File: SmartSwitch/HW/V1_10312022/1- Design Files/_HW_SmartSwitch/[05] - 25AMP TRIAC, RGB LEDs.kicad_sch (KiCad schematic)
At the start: 6 parts

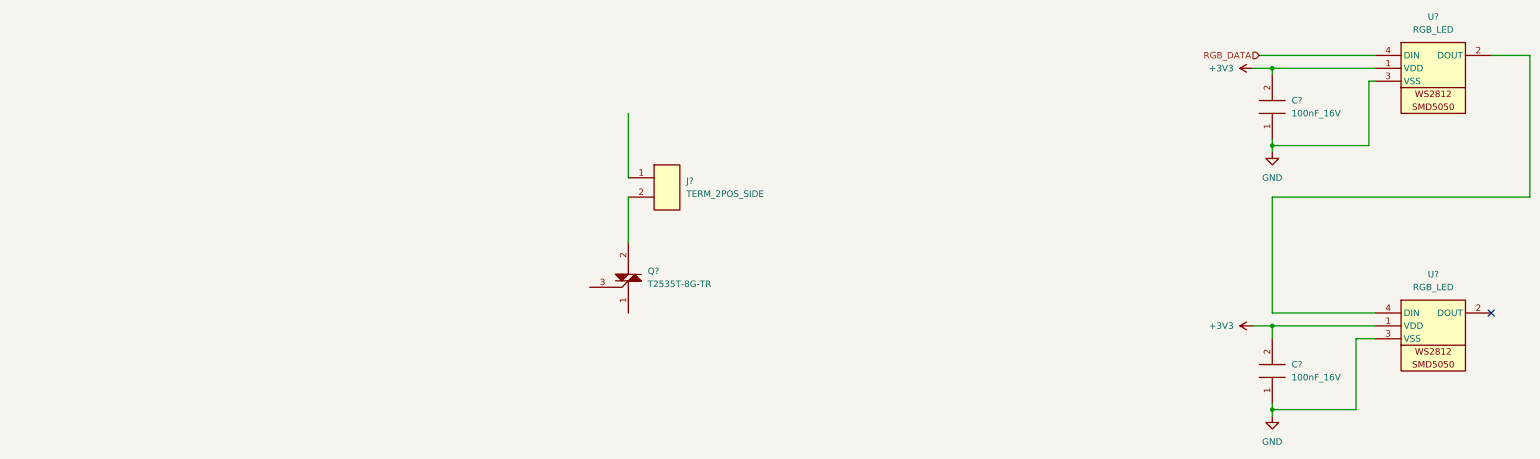
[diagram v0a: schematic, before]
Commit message: Current sensor has been done almost :D
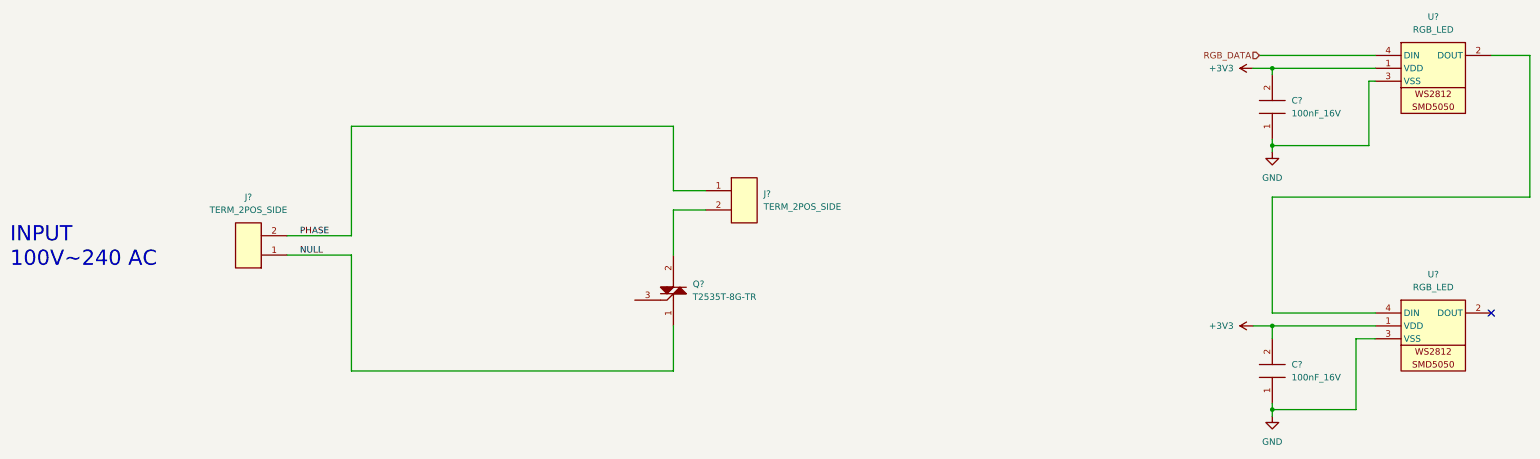
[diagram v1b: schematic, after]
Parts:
- added J?: TERM_2POS_SIDE, TerminalBlock_Phoenix:TerminalBlock_Phoenix_MKDS-1,5-2_1x02_P5.00mm_Horizontal, symbol SmartSwitch:TERM_2POS_SIDE
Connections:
- net PHASE: now reaches J?.1
- net PHASE: now also J?.2
- net NULL: now reaches Q?.1
- net NULL: now also J?.1
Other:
- note added: "INPUT 100V~240 AC"
- moved on the sheet: J?, Q?
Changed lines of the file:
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@@
   )
   (no_connect (at 335.28 149.86))
+  (wire (pts (xy 97.79 134.62) (xy 110.49 134.62))
+    (stroke (width 0) (type default) (color 0 0 0 0))
+  )
   (wire (pts (xy 289.56 99.06) (xy 312.42 99.06))
     (stroke (width 0) (type default) (color 0 0 0 0))
   )
+  (wire (pts (xy 180.34 125.73) (xy 173.99 125.73))
+    (stroke (width 0) (type default) (color 0 0 0 0))
+  )
   (wire (pts (xy 311.15 116.84) (xy 292.1 116.84))
     (stroke (width 0) (type default) (color 0 0 0 0))
   )
+  (wire (pts (xy 110.49 134.62) (xy 110.49 113.03))
+    (stroke (width 0) (type default) (color 0 0 0 0))
+  )
   (wire (pts (xy 292.1 149.86) (xy 312.42 149.86))
     (stroke (width 0) (type default) (color 0 0 0 0))
@@
     (stroke (width 0) (type default) (color 0 0 0 0))
   )
-  (wire (pts (xy 165.1 110.49) (xy 165.1 123.19))
+  (wire (pts (xy 173.99 125.73) (xy 173.99 113.03))
+    (stroke (width 0) (type default) (color 0 0 0 0))
+  )
+  (wire (pts (xy 110.49 161.29) (xy 173.99 161.29))
     (stroke (width 0) (type default) (color 0 0 0 0))
   )
@@
     (stroke (width 0) (type default) (color 0 0 0 0))
   )
-  (wire (pts (xy 165.1 127) (xy 165.1 135.89))
-    (stroke (width 0) (type default) (color 0 0 0 0))
-  )
   (wire (pts (xy 342.9 127) (xy 292.1 127))
     (stroke (width 0) (type default) (color 0 0 0 0))
   )
+  (wire (pts (xy 97.79 138.43) (xy 110.49 138.43))
+    (stroke (width 0) (type default) (color 0 0 0 0))
+  )
+  (wire (pts (xy 173.99 161.29) (xy 173.99 152.4))
+    (stroke (width 0) (type default) (color 0 0 0 0))
+  )
+  (wire (pts (xy 180.34 129.54) (xy 173.99 129.54))
+    (stroke (width 0) (type default) (color 0 0 0 0))
+  )
   (wire (pts (xy 312.42 104.14) (xy 311.15 104.14))
     (stroke (width 0) (type default) (color 0 0 0 0))
@@
     (stroke (width 0) (type default) (color 0 0 0 0))
   )
+  (wire (pts (xy 173.99 129.54) (xy 173.99 138.43))
+    (stroke (width 0) (type default) (color 0 0 0 0))
+  )
   (wire (pts (xy 288.29 152.4) (xy 292.1 152.4))
     (stroke (width 0) (type default) (color 0 0 0 0))
   )
+  (wire (pts (xy 110.49 113.03) (xy 173.99 113.03))
+    (stroke (width 0) (type default) (color 0 0 0 0))
+  )
   (wire (pts (xy 335.28 99.06) (xy 342.9 99.06))
     (stroke (width 0) (type default) (color 0 0 0 0))
@@
   (wire (pts (xy 292.1 101.6) (xy 292.1 102.87))
     (stroke (width 0) (type default) (color 0 0 0 0))
+  )
+  (wire (pts (xy 110.49 138.43) (xy 110.49 161.29))
+    (stroke (width 0) (type default) (color 0 0 0 0))
+  )
+  (text "INPUT\n100V~240 AC\n" (at 43.18 140.97 0)
+    (effects (font (size 3 3)) (justify left bottom))
+  )
+  (label "PHASE" (at 100.33 134.62 0)
+    (effects (font (size 1.27 1.27)) (justify left bottom))
+  )
+  (label "NULL" (at 100.33 138.43 0)
+    (effects (font (size 1.27 1.27)) (justify left bottom))
   )
   (hierarchical_label "RGB_DATA" (shape input) (at 289.56 99.06 180)
@@
     (pin "4")
   )
+  (symbol (lib_id "SmartSwitch:TERM_2POS_SIDE") (at 92.71 140.97 180) (unit 1)
+    (in_bom yes) (on_board yes) (fields_autoplaced)
+    (property "Reference" "J?" (id 0) (at 90.17 127 0))
+    (property "Value" "TERM_2POS_SIDE" (id 1) (at 90.17 129.54 0))
+    (property "Footprint" "TerminalBlock_Phoenix:TerminalBlock_Phoenix_MKDS-1,5-2_1x02_P5.00mm_Horizontal" (id 2) (at 50.8 151.13 0)
+      (effects (font (size 1.27 1.27)) hide)
+    )
+    (property "Datasheet" "https://www.we-online.com/katalog/datasheet/691137710002.pdf" (id 3) (at 60.96 146.05 0)
+      (effects (font (size 1.27 1.27)) hide)
+    )
+    (property "Description" "TERM BLK 2POS SIDE ENTRY 5MM PCB" (id 4) (at 74.93 148.59 0)
+      (effects (font (size 1.27 1.27)) hide)
+    )
+    (pin "1")
+    (pin "2")
+  )
   (symbol (lib_id "power:GND") (at 292.1 118.11 0) (unit 1)
     (in_bom yes) (on_board yes) (fields_autoplaced)
@@
     (pin "1")
   )
-  (symbol (lib_id "SmartSwitch:TERM_2POS_SIDE") (at 170.18 120.65 0) (unit 1)
-    (in_bom yes) (on_board yes) (fields_autoplaced)
-    (property "Reference" "J?" (id 0) (at 176.53 123.8249 0)
-      (effects (font (size 1.27 1.27)) (justify left))
-    )
-    (property "Value" "TERM_2POS_SIDE" (id 1) (at 176.53 126.3649 0)
-      (effects (font (size 1.27 1.27)) (justify left))
-    )
-    (property "Footprint" "TerminalBlock_Phoenix:TerminalBlock_Phoenix_MKDS-1,5-2_1x02_P5.00mm_Horizontal" (id 2) (at 212.09 110.49 0)
-      (effects (font (size 1.27 1.27)) hide)
-    )
-    (property "Datasheet" "https://www.we-online.com/katalog/datasheet/691137710002.pdf" (id 3) (at 201.93 115.57 0)
-      (effects (font (size 1.27 1.27)) hide)
-    )
-    (property "Description" "TERM BLK 2POS SIDE ENTRY 5MM PCB" (id 4) (at 187.96 113.03 0)
-      (effects (font (size 1.27 1.27)) hide)
-    )
-    (pin "1")
-    (pin "2")
-  )
-  (symbol (lib_id "SmartSwitch:T2535T-8G-TR") (at 157.48 135.89 0) (unit 1)
-    (in_bom yes) (on_board yes) (fields_autoplaced)
-    (property "Reference" "Q?" (id 0) (at 168.91 141.6049 0)
-      (effects (font (size 1.27 1.27)) (justify left))
-    )
-    (property "Value" "T2535T-8G-TR" (id 1) (at 168.91 144.1449 0)
-      (effects (font (size 1.27 1.27)) (justify left))
-    )
-    (property "Footprint" "Package_TO_SOT_SMD:TO-263-2" (id 2) (at 173.99 123.19 0)
-      (effects (font (size 1.27 1.27)) hide)
-    )
-    (property "Datasheet" "https://www.st.com/resource/en/datasheet/t2535t-8g.pdf" (id 3) (at 186.69 125.73 0)
-      (effects (font (size 1.27 1.27)) hide)
-    )
-    (property "Description" "TRIAC Standard 800 V 25 A Surface Mount D²PAK" (id 4) (at 181.61 128.27 0)
-      (effects (font (size 1.27 1.27)) hide)
-    )
+  (symbol (lib_id "SmartSwitch:TERM_2POS_SIDE") (at 185.42 123.19 0) (unit 1)
+    (in_bom yes) (on_board yes) (fields_autoplaced)
+    (property "Reference" "J?" (id 0) (at 191.77 126.3649 0)
+      (effects (font (size 1.27 1.27)) (justify left))
+    )
+    (property "Value" "TERM_2POS_SIDE" (id 1) (at 191.77 128.9049 0)
+      (effects (font (size 1.27 1.27)) (justify left))
+    )
+    (property "Footprint" "TerminalBlock_Phoenix:TerminalBlock_Phoenix_MKDS-1,5-2_1x02_P5.00mm_Horizontal" (id 2) (at 227.33 113.03 0)
+      (effects (font (size 1.27 1.27)) hide)
+    )
+    (property "Datasheet" "https://www.we-online.com/katalog/datasheet/691137710002.pdf" (id 3) (at 217.17 118.11 0)
+      (effects (font (size 1.27 1.27)) hide)
+    )
+    (property "Description" "TERM BLK 2POS SIDE ENTRY 5MM PCB" (id 4) (at 203.2 115.57 0)
+      (effects (font (size 1.27 1.27)) hide)
+    )
+    (pin "1")
+    (pin "2")
+  )
+  (symbol (lib_id "SmartSwitch:T2535T-8G-TR") (at 166.37 138.43 0) (unit 1)
+    (in_bom yes) (on_board yes) (fields_autoplaced)
+    (property "Reference" "Q?" (id 0) (at 177.8 144.1449 0)
+      (effects (font (size 1.27 1.27)) (justify left))
+    )
+    (property "Value" "T2535T-8G-TR" (id 1) (at 177.8 146.6849 0)
+      (effects (font (size 1.27 1.27)) (justify left))
+    )
+    (property "Footprint" "Package_TO_SOT_SMD:TO-263-2" (id 2) (at 182.88 125.73 0)
+      (effects (font (size 1.27 1.27)) hide)
+    )
+    (property "Datasheet" "https://www.st.com/resource/en/datasheet/t2535t-8g.pdf" (id 3) (at 195.58 128.27 0)
+      (effects (font (size 1.27 1.27)) hide)
+    )
+    (property "Description" "TRIAC Standard 800 V 25 A Surface Mount D²PAK" (id 4) (at 190.5 130.81 0)
+      (effects (font (size 1.27 1.27)) hide)
+    )

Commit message: Current and Voltage sampler
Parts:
- removed C? (x2): 100nF_16V, Capacitor_SMD:C_0402_1005Metric, symbol SmartSwitch:100nF_16V
- removed J? (x2): TERM_2POS_SIDE, TerminalBlock_Phoenix:TerminalBlock_Phoenix_MKDS-1,5-2_1x02_P5.00mm_Horizontal, symbol SmartSwitch:TERM_2POS_SIDE
- removed Q?: T2535T-8G-TR, Package_TO_SOT_SMD:TO-263-2, symbol SmartSwitch:T2535T-8G-TR
- removed U? (x2): RGB_LED, LED_SMD:LED_WS2812B_PLCC4_5.0x5.0mm_P3.2mm, symbol SmartSwitch:RGB_LED
- added J?: IEC-EW-4, symbol SmartSwitch:IEC-EW-4
- added J?: PX0675/PC, symbol SmartSwitch:PX0675/PC
- added Q?: T2535T-8G-TR, Package_TO_SOT_SMD:TO-263-2, symbol SmartSwitch:T2535T-8G-TR
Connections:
- net NULL: now also J?.3 (N), J?.3 (N)
- net PHASE: now also J?.1 (L)
- new net: J?.1 (L), Q?.1
- new net CURRENT SENS/L_OUT: Q?.2
- new net EARTH: J?.2 (E), J?.2 (E)
- no-connect marks 1 -> 0
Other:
- added sheet CURRENT SENS ([05]-CURRENT SENSOR.kicad_sch)
- note added: "INPUT 85~250 AC 10A MAX"
- note removed: "INPUT 100V~240 AC"
